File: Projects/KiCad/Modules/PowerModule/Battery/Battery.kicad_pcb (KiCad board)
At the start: 2 copper layers, 110 x 95 mm, 15 parts, among them J1 Conn_01x02_Socket

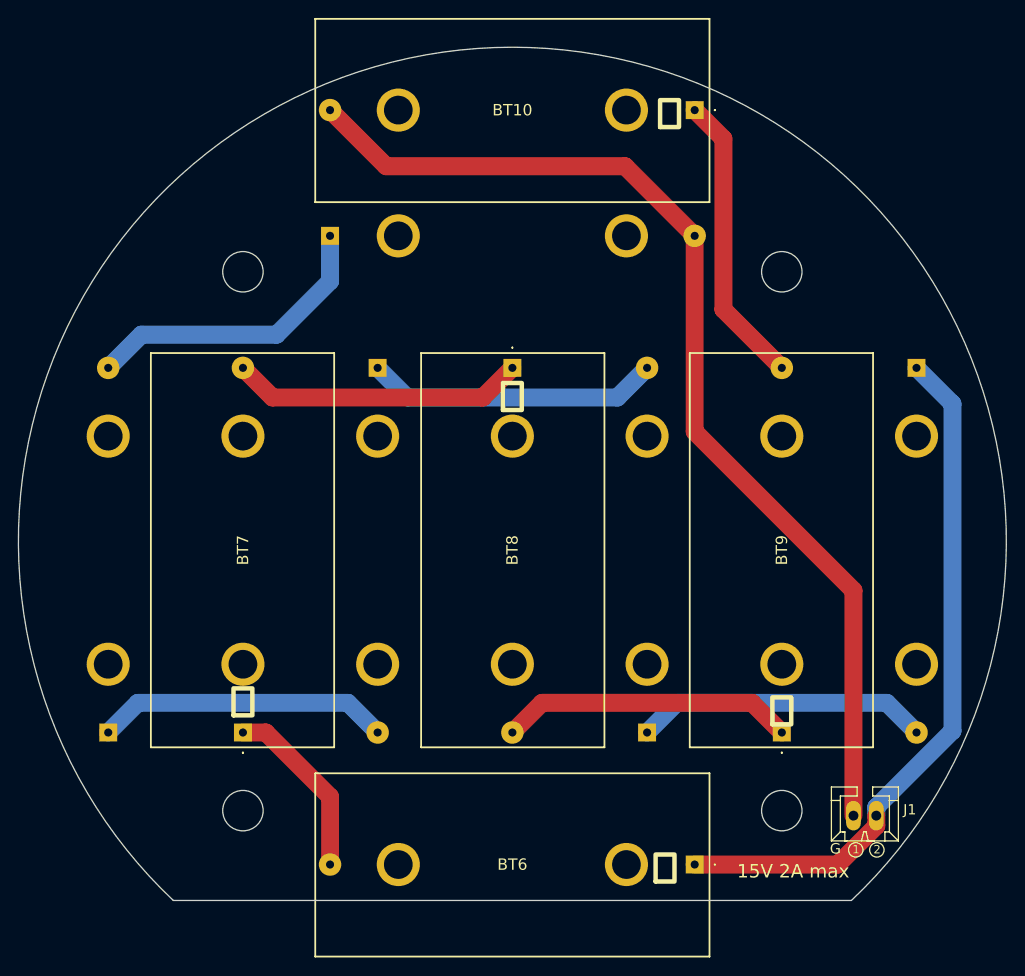
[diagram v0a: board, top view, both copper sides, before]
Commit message: コネクタ位置を揃えた
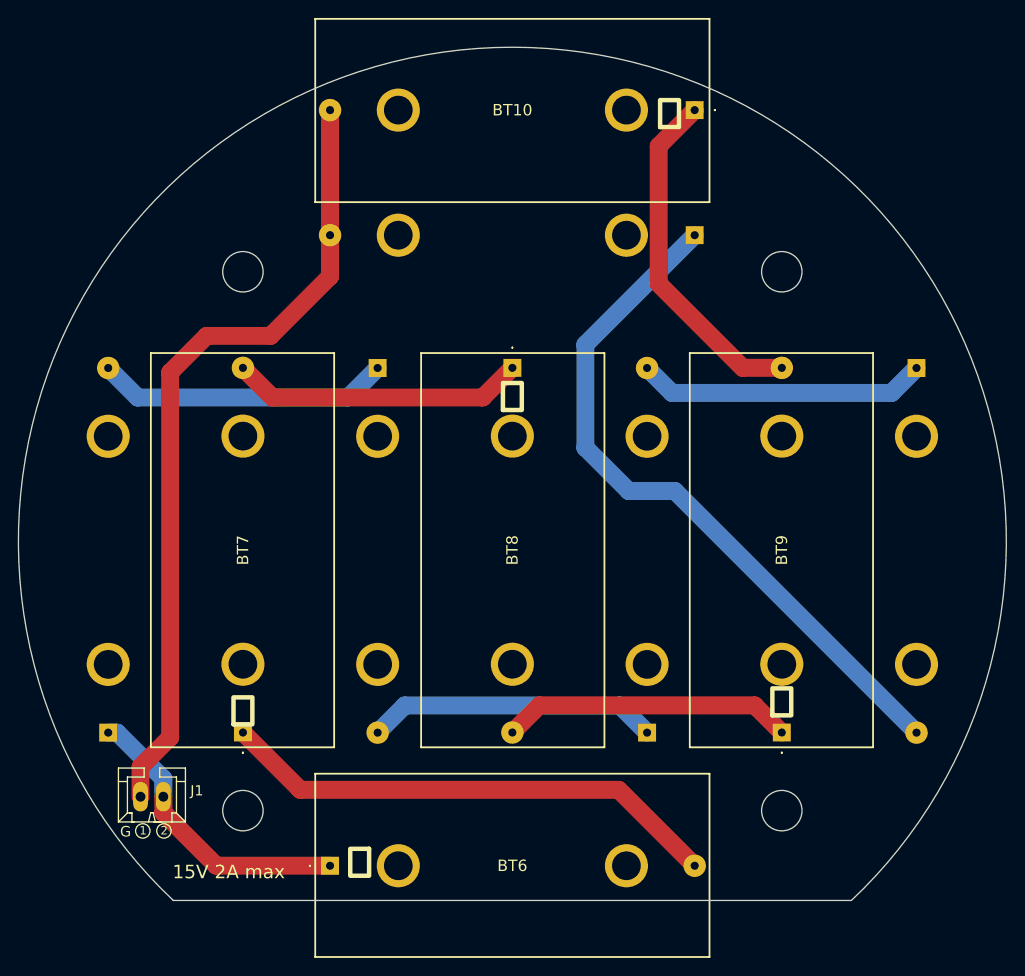
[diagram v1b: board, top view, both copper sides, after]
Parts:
- moved BT1 98.7 mm to (99.8, 119.1), turned to 90 degrees
- moved BT4 98.7 mm to (189.8, 78.5), turned to -90 degrees
- moved J1 79.4 mm to (104.6, 126.2)
- moved BT3 50.5 mm to (159.8, 119.1), turned to 90 degrees
- moved BT2 50.5 mm to (129.8, 78.5), turned to -90 degrees
- moved BT6 40.6 mm to (124.5, 133.9), turned to 0 degrees
- moved BT5 40.6 mm to (165.1, 63.7), turned to 180 degrees
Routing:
- net Net-(BT1-+): track 78.2 -> 33.1 mm
- net Net-(BT4--): track 33.7 -> 78.7 mm
- net Net-(BT6--): track 20.2 -> 56.4 mm
- net Net-(BT10--): track 118.3 -> 89.4 mm
- net Net-(BT10-+): track 32.7 -> 38.6 mm
